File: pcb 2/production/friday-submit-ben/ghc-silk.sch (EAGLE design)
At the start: 59 parts, among them IC1 ATMEGA168TQFP-08, IC2 7805DT, IC4 L298, J1 POWER_JACKPTH, K2 G5LE, Q1 MMBT2222A, SW2 MOMENTARYBUTTON, U1 L298HEATSINK

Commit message: Fixed Traces
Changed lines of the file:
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@@
 <net name="COMMON" class="0">
 <segment>
-<label x="91.44" y="147.32" size="1.778" layer="95" rot="R180"/>
+<label x="93.98" y="154.94" size="1.778" layer="95" rot="R180"/>
 <pinref part="J3" gate="J$1" pin="1"/>
-<wire x1="93.98" y1="147.32" x2="96.52" y2="152.4" width="0.1524" layer="91"/>
+<wire x1="93.98" y1="154.94" x2="96.52" y2="152.4" width="0.1524" layer="91"/>
 </segment>
 <segment>

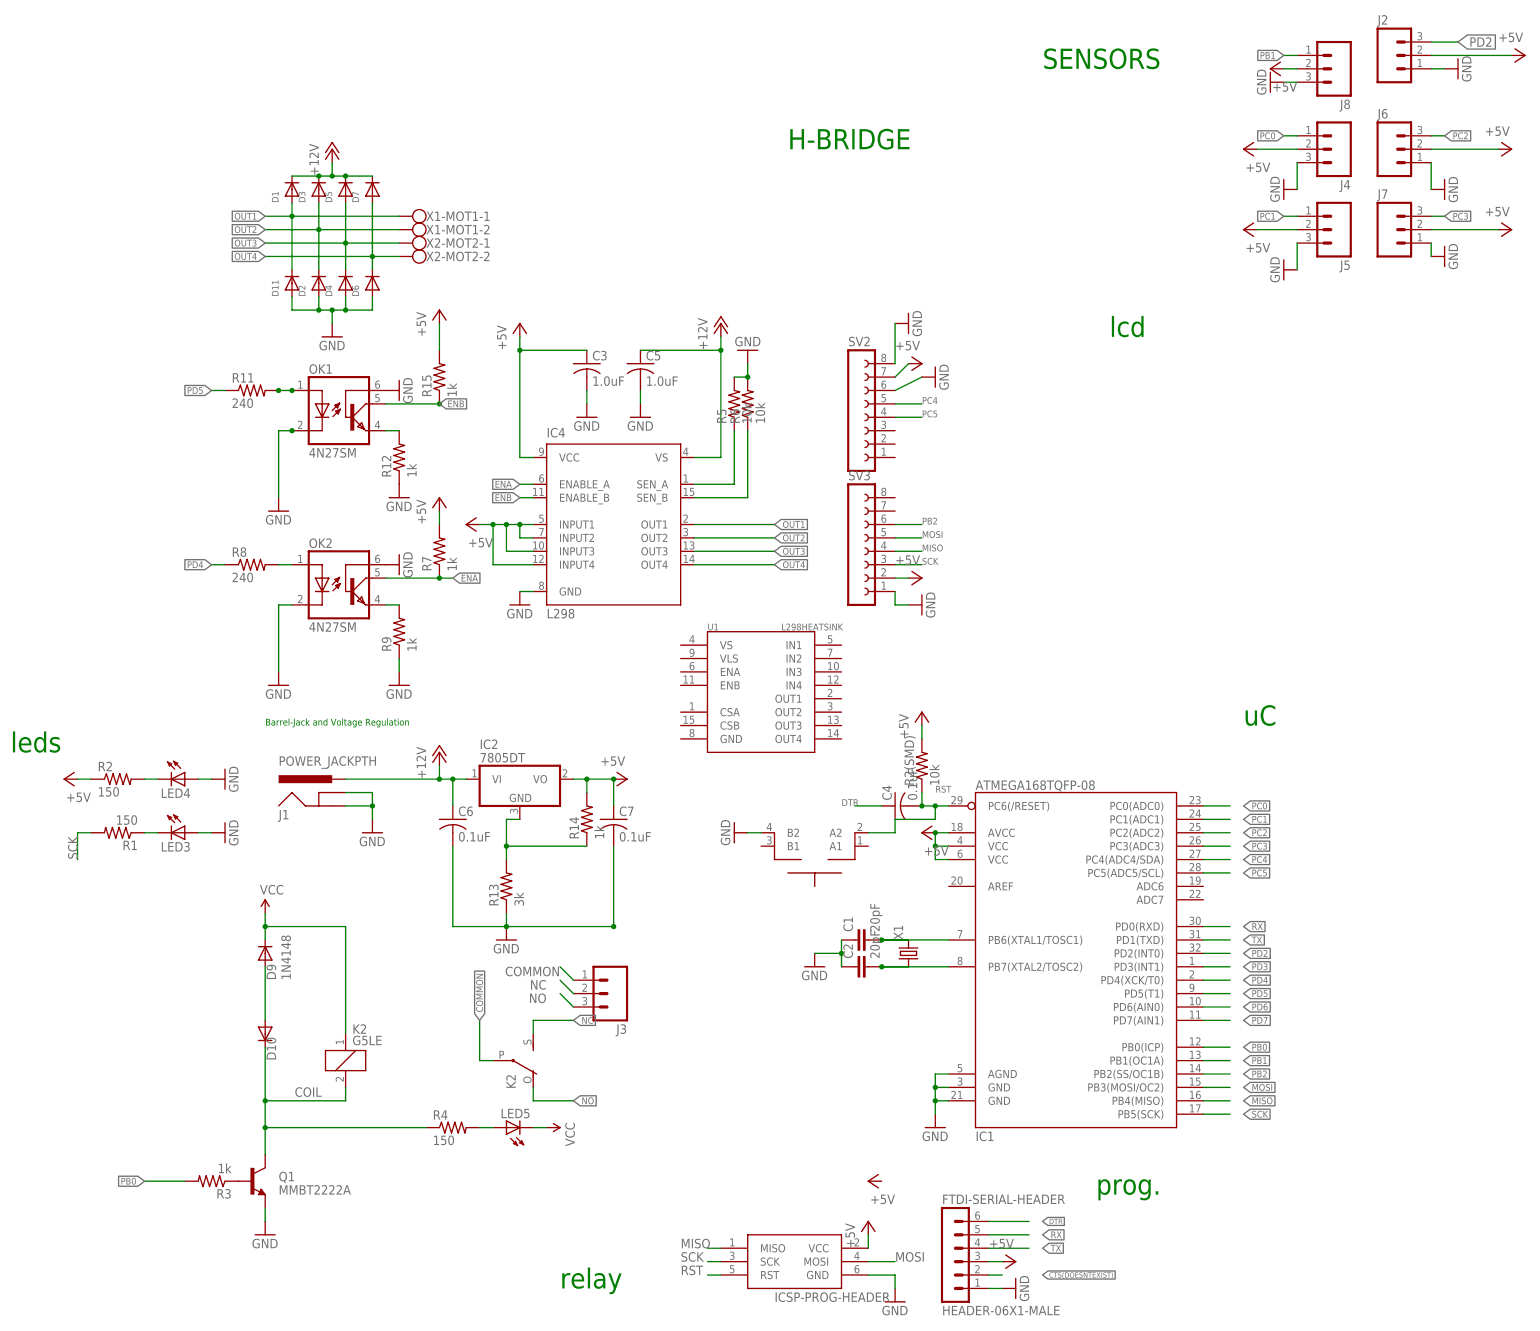
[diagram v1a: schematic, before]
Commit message: Replaced H-bridge, remapped pins where needed. Needs routing still
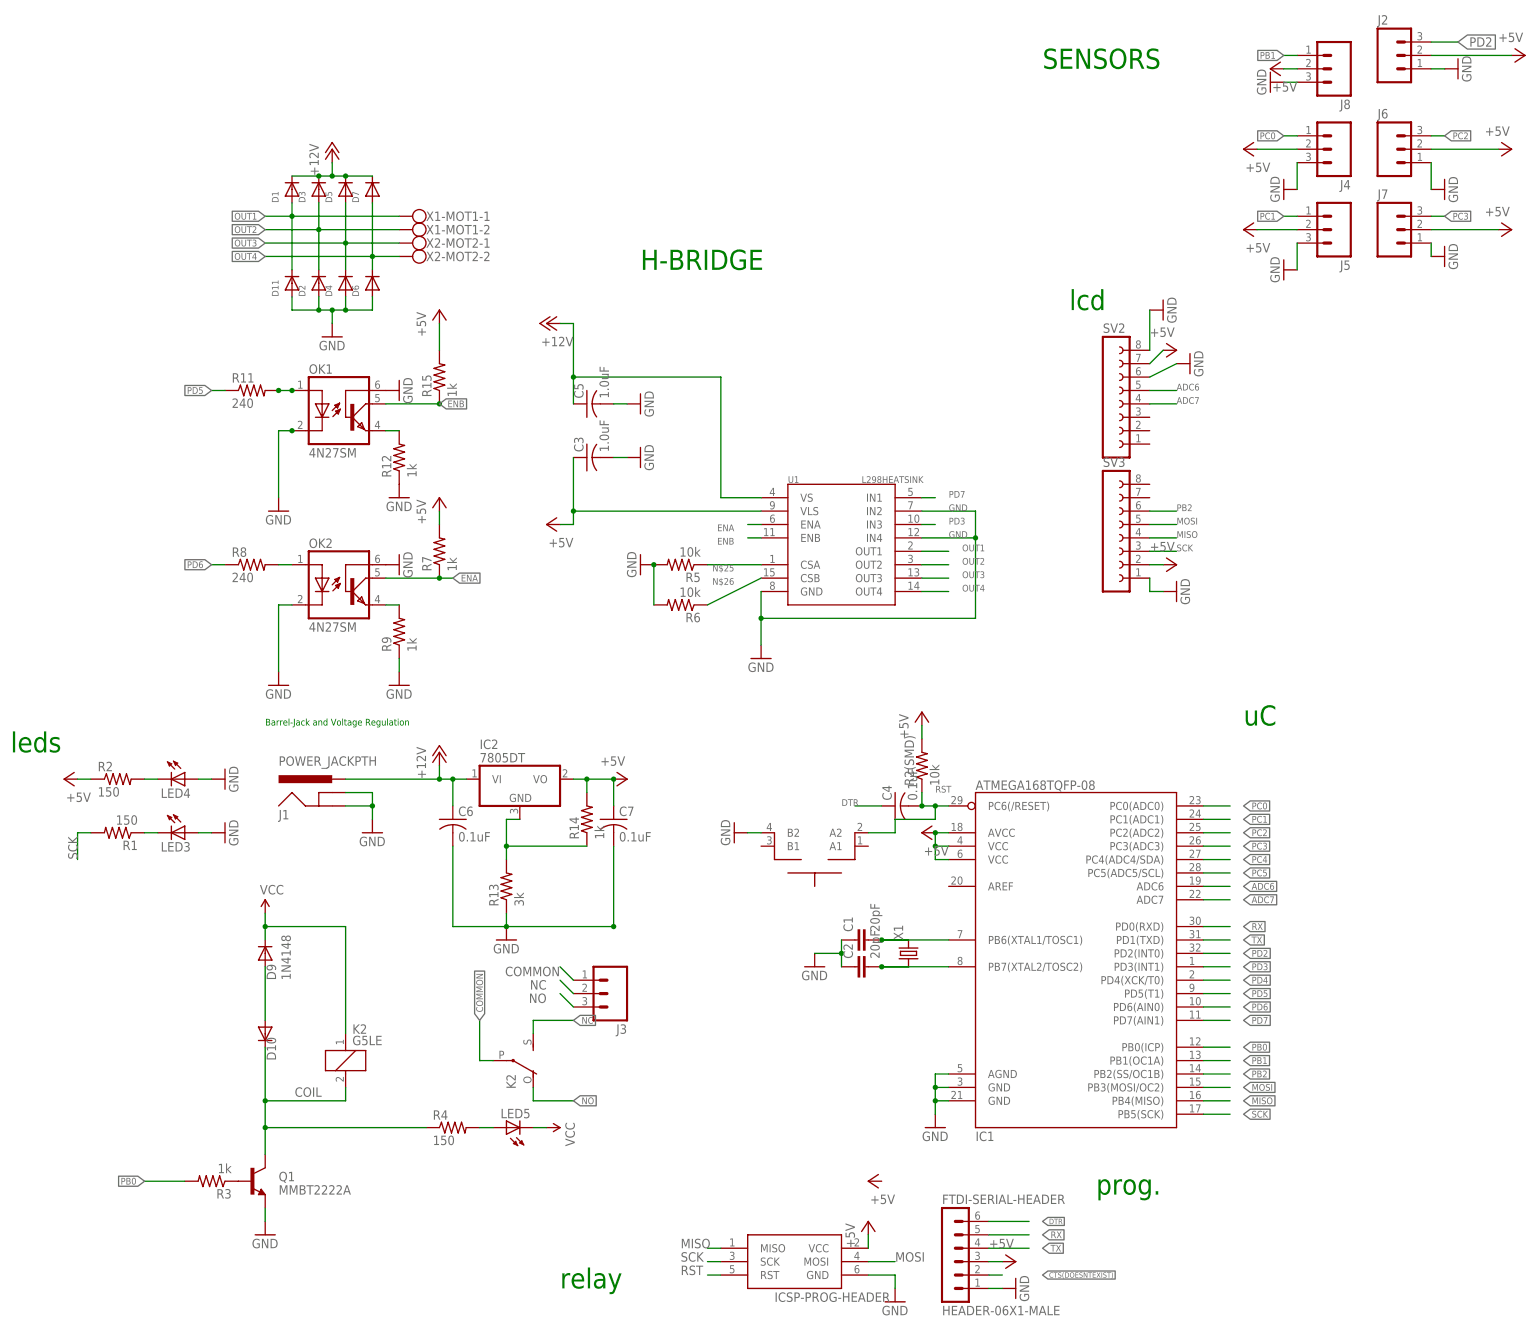
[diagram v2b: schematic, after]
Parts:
- removed IC4: L298, st-microelectronics:L298
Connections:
- removed net SEN_A: IC4.SEN_A, R5.1
- removed net SEN_B: IC4.SEN_B, R6.1
- new net ADC6: IC1.ADC6, SV2.5
- new net ADC7: IC1.ADC7, SV2.4
- new net N$25: R5.1, U1.CSA
- new net N$26: R6.1, U1.CSB
- net +12V: now also U1.VS; no longer IC4.VS
- net +5V: now also U1.VLS; no longer IC4.INPUT1, IC4.INPUT2, IC4.INPUT3, IC4.INPUT4, IC4.VCC
- net ENA: now also U1.ENA; no longer IC4.ENABLE_A
- net ENB: now also U1.ENB; no longer IC4.ENABLE_B
- net GND: now also U1.GND, U1.IN2, U1.IN4; no longer IC4.GND
- net OUT1: now also U1.OUT1; no longer IC4.OUT1
- net OUT2: now also U1.OUT2; no longer IC4.OUT2
- net OUT3: now also U1.OUT3; no longer IC4.OUT3
- net OUT4: now also U1.OUT4; no longer IC4.OUT4
- net PC4: no longer SV2.5
- net PC5: no longer SV2.4
- net PD3: now also U1.IN3
- net PD4: no longer R8.1
- net PD6: now also R8.1
- net PD7: now also U1.IN1
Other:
- moved on the sheet: C3, C5, R5, R6, SV2, SV3, U1
